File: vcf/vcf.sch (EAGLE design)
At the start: 98 parts, among them IC1 OPA4130U, IC2 OPA4130U, IC3 OPA4130U, IC4 OPA4130U, IC5 OPA4130U, Q1 BC847ASMD, Q2 BC847ASMD, Q3 BC847ASMD, Q4 BC847ASMD, Q5 BC847ASMD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

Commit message: made bug fixes.  almost ready to send out again.
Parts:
- removed R21, R27, R28, R43: 1meg, dan:R-US_R0603
- C1: value 1n -> 18n
- C2, C3, C4: value 1n -> 36n
- R23: value 100k -> 10k
- R25, R26: value 10k -> 1k
- R44: value 10k -> 100k
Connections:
- removed net N$43: IC1D.+IN, R43.2, VPEROCT.P$3
- new net N$67: AIN.P$3, GAIN.E
- net GND: no longer R21.1, R27.1, R28.1, R43.1
- net N$18: now also AIN2.P$3, GAIN1.E; no longer AIN.P$3, IC1A.+IN, R21.2
- net N$29: now also R25.1; no longer MODAMT.E
- net N$30: now also R20.1; no longer GAIN1.E
- net N$33: now also MIN.P$3, MODAMT.E; no longer AIN2.P$3, IC1B.+IN, R27.2
- net N$38: now also R26.1; no longer SCALE.E
- net N$40: now also SCALE.E, VPEROCT.P$3; no longer MODAMT.S, R25.1
- net N$41: now also IC1D.+IN; no longer R26.1
- net N$50: now also MODAMT.S; no longer MIN.P$3, R28.2
- net N$57: now also IC1A.+IN; no longer R19.1
- net N$62: now also IC1B.+IN; no longer R20.1
- net N$63: now also R19.1; no longer GAIN.E
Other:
- note added: "make this res bigger"
- note removed: "Freq pot polarity is wrong"
- note removed: "Move the buffers after the pots"
- moved on the sheet: GAIN, GAIN1, IC1A, IC1B, IC1C, IC1D, MODAMT, SCALE

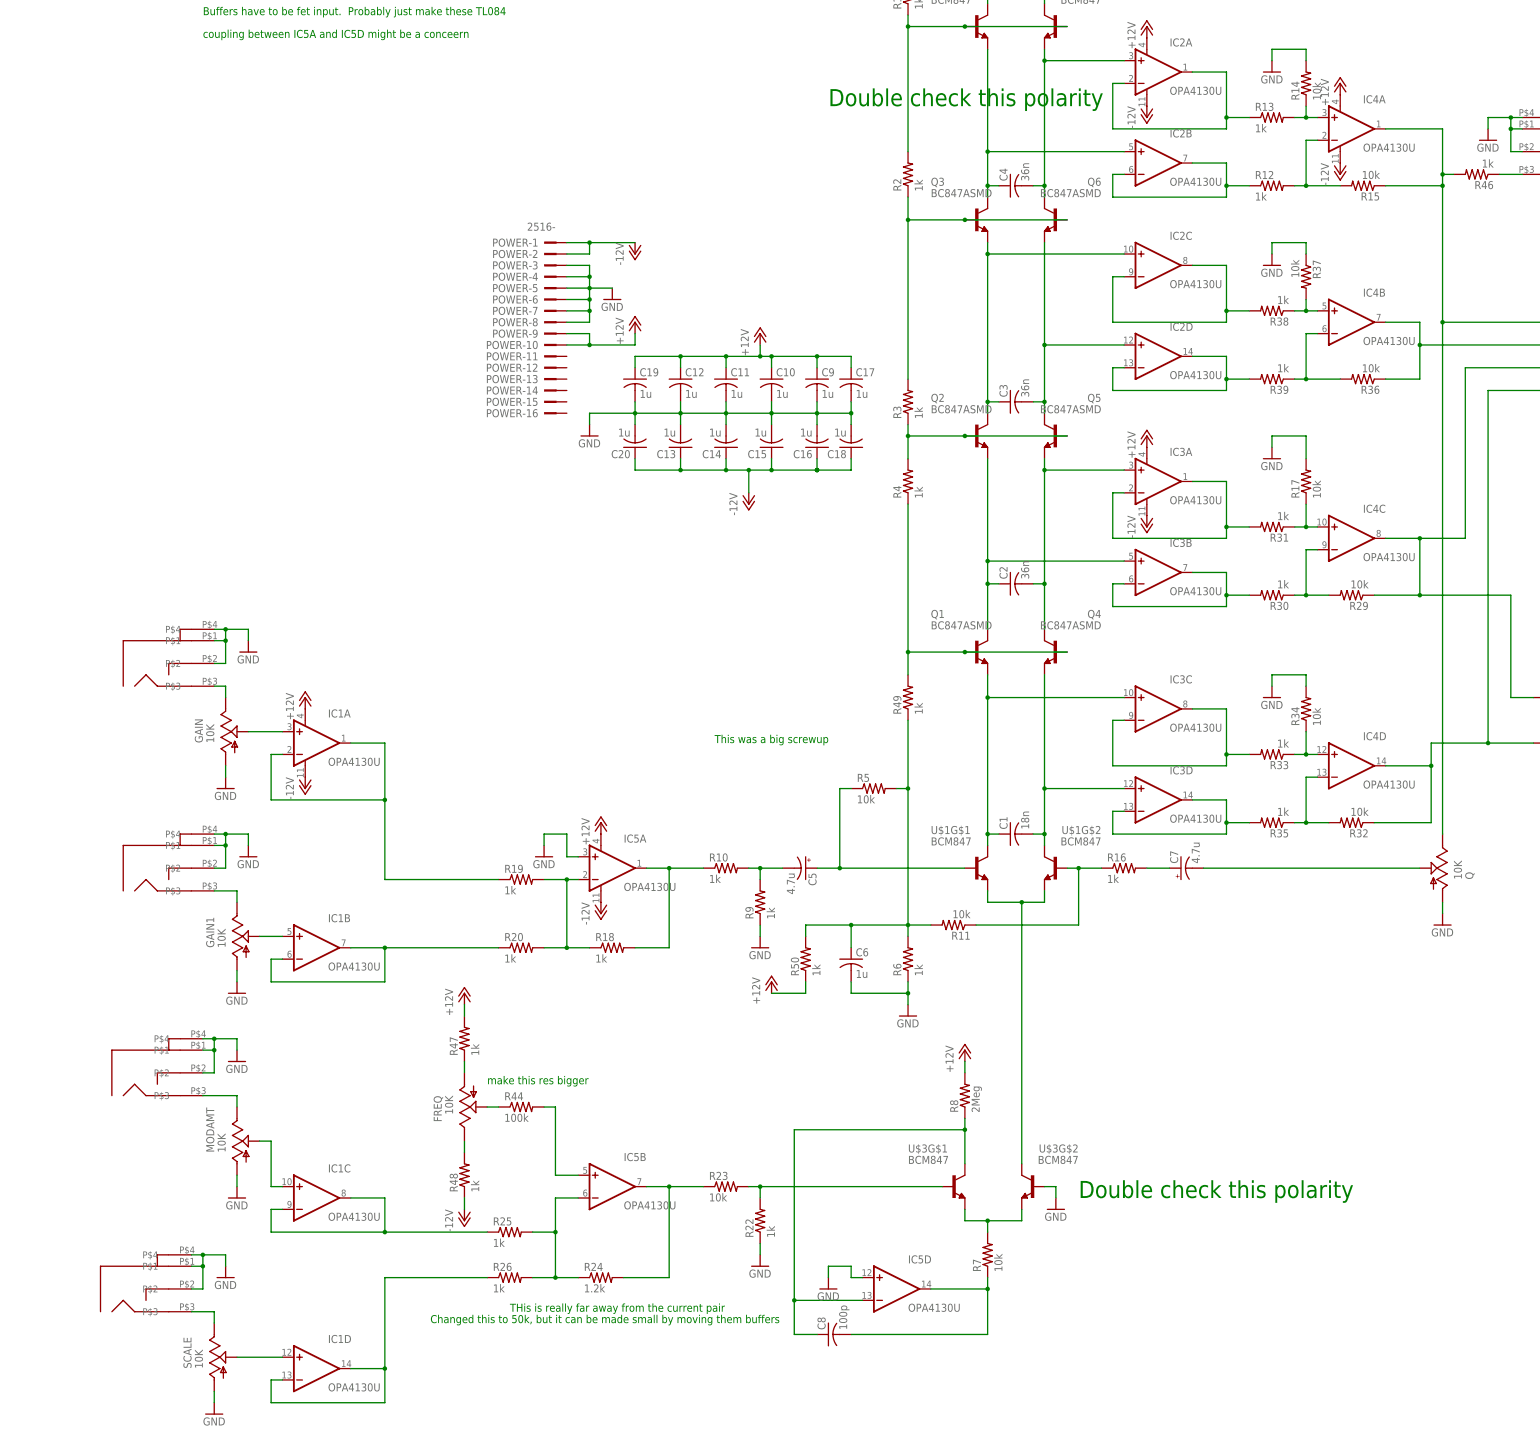
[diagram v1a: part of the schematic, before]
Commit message: fixed the input impedance situation.
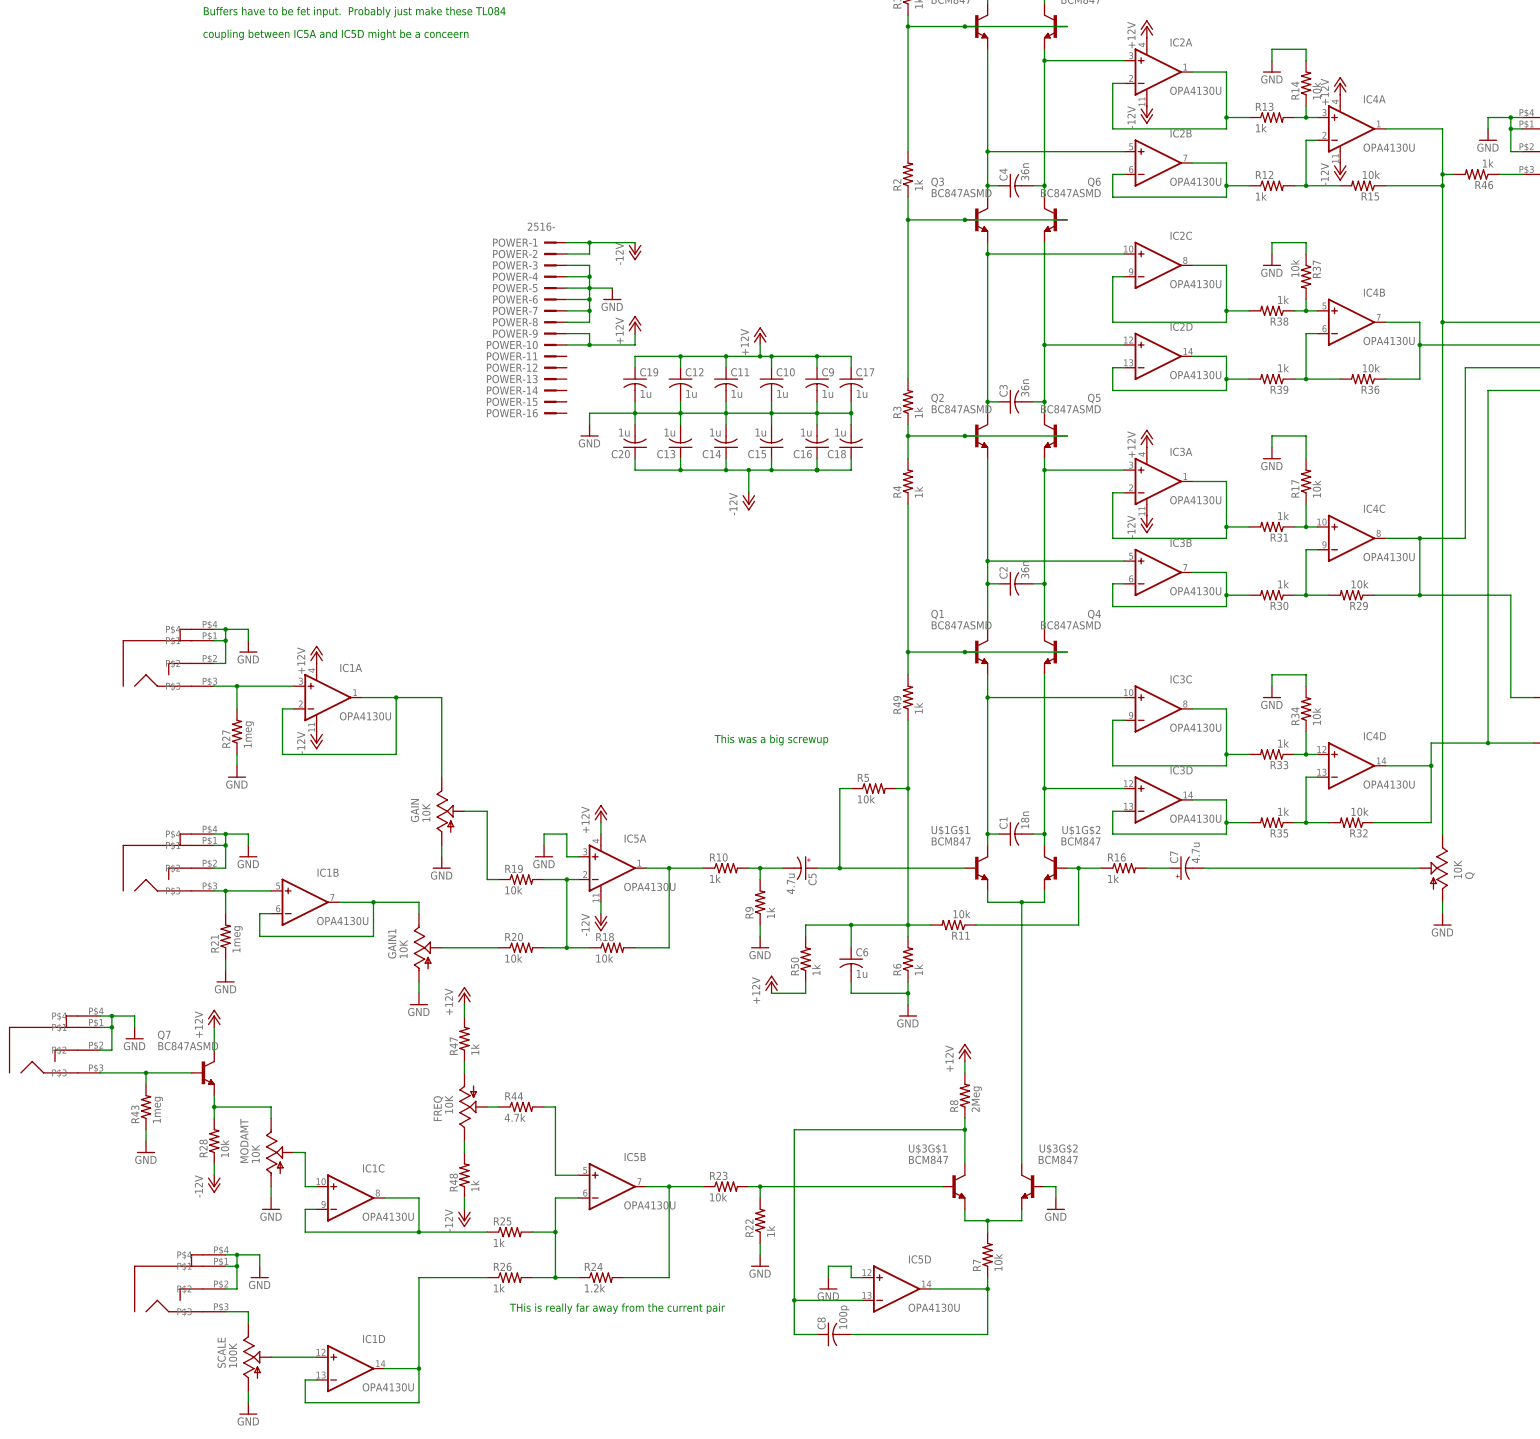
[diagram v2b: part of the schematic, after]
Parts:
- added Q7: BC847ASMD, dan:BC847ASMD
- added R21, R27, R43: 1meg, dan:R-US_R0603
- added R28: 10k, dan:R-US_R0603
- R18, R19, R20: value 1k -> 10k
- R44: value 100k -> 4.7k
- SCALE: value 10K -> 100K
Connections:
- removed net N$63: IC1A.-IN, IC1A.OUT, R19.1
- new net N$43: GAIN.S, R19.1
- new net N$69: AIN2.P$3, IC1B.+IN, R21.2
- net +12V: now also Q7.C
- net -12V: now also R28.1
- net GND: now also R21.1, R27.1, R43.1
- net N$18: now also MIN.P$3, Q7.B, R43.2; no longer AIN2.P$3, GAIN1.E
- net N$30: now also GAIN1.E; no longer R20.1
- net N$33: now also Q7.E, R28.2; no longer MIN.P$3
- net N$57: now also GAIN1.S, R20.1; no longer GAIN.S, IC1A.+IN
- net N$62: now also AIN.P$3, IC1A.+IN, R27.2; no longer GAIN1.S, IC1B.+IN
- net N$67: now also IC1A.-IN, IC1A.OUT; no longer AIN.P$3
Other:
- note removed: "Changed this to 50k, but it can be made small by moving them buffers"
- note removed: "Double check this polarity"
- note removed: "make this res bigger"
- moved on the sheet: GAIN, GAIN1, IC1A, IC1B, IC1C, IC1D, MODAMT, SCALE

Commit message: fixed values in schematic after getting 2nd board rev back.
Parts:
- R10: value 1k -> 10k
- R25: value 1k -> 2.2k
- R26: value 1k -> 4.7k
- R44: value 4.7k -> 10k
- R47, R48: value 1k -> 100k
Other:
- note added: "100k might be a good value for these"
- note removed: "THis is really far away from the current pair"
- note removed: "This was a big screwup"
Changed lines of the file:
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@@
 <part name="R9" library="dan" deviceset="R-US_" device="R0603" value="1k"/>
 <part name="GND4" library="dan" deviceset="GND" device=""/>
-<part name="R10" library="dan" deviceset="R-US_" device="R0603" value="1k"/>
+<part name="R10" library="dan" deviceset="R-US_" device="R0603" value="10k"/>
 <part name="R11" library="dan" deviceset="R-US_" device="R0603" value="10k"/>
 <part name="P+3" library="dan" deviceset="+12V" device=""/>
@@
 <part name="R23" library="dan" deviceset="R-US_" device="R0603" value="10k"/>
 <part name="R24" library="dan" deviceset="R-US_" device="R0603" value="1.2k"/>
-<part name="R25" library="dan" deviceset="R-US_" device="R0603" value="1k"/>
-<part name="R26" library="dan" deviceset="R-US_" device="R0603" value="1k"/>
+<part name="R25" library="dan" deviceset="R-US_" device="R0603" value="2.2k"/>
+<part name="R26" library="dan" deviceset="R-US_" device="R0603" value="4.7k"/>
 <part name="MODAMT" library="dan" deviceset="US-EVU" device="F2J" value="10K"/>
 <part name="GND11" library="dan" deviceset="GND" device=""/>
@@
 <part name="P-7" library="dan" deviceset="-12V" device=""/>
 <part name="P+9" library="dan" deviceset="+12V" device=""/>
-<part name="R44" library="dan" deviceset="R-US_" device="R0603" value="4.7k"/>
+<part name="R44" library="dan" deviceset="R-US_" device="R0603" value="10k"/>
 <part name="GAIN1" library="dan" deviceset="US-EVU" device="F2J" value="10K"/>
 <part name="C5" library="dan" deviceset="CPOL-US" device="E2.5-6" value="4.7u"/>
@@
 <part name="R45" library="dan" deviceset="R-US_" device="R0603" value="1k"/>
 <part name="R46" library="dan" deviceset="R-US_" device="R0603" value="1k"/>
-<part name="R47" library="dan" deviceset="R-US_" device="R0603" value="1k"/>
-<part name="R48" library="dan" deviceset="R-US_" device="R0603" value="1k"/>
+<part name="R47" library="dan" deviceset="R-US_" device="R0603" value="100k"/>
+<part name="R48" library="dan" deviceset="R-US_" device="R0603" value="100k"/>
 <part name="R49" library="dan" deviceset="R-US_" device="R0603" value="1k"/>
 <part name="P+11" library="dan" deviceset="+12V" device=""/>
@@
 <text x="-137.16" y="228.6" size="1.778" layer="91">Buffers have to be fet input.  Probably just make these TL084</text>
 <text x="-137.16" y="223.52" size="1.778" layer="91">coupling between IC5A and IC5D might be a conceern</text>
-<text x="-68.58" y="-60.96" size="1.778" layer="91">THis is really far away from the current pair</text>
-<text x="-22.86" y="66.04" size="1.778" layer="91">This was a big screwup</text>
+<text x="-73.66" y="-2.54" size="1.778" layer="91">100k might be a good value for these</text>
 </plain>
 <instances>

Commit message: added a vca.  made changes to the filter components
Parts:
- added C21, C22: 10u, dan:CPOL-USE2.5-6
- added R51: 10, dan:R-US_R0603
- C5: value 4.7u -> 10u
- R10, R14, R15, R17, R19, R20, R29, R32, R34, R36, R37: value 10k -> 47k
- R44: value 10k -> 470k
- R47, R48: value 100k -> 22k
- R50: value 1k -> dnp
- R9: value 1k -> 10
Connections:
- new net N$63: C21.+, R46.2
- new net N$70: C22.+, R45.2
- new net N$71: POWER-10.KL, POWER-9.KL, R51.2
- new net N$72: POWER-1.KL, POWER-2.KL, R9.2
- net +12V: now also R51.1; no longer POWER-10.KL, POWER-9.KL
- net -12V: now also R9.1; no longer POWER-1.KL, POWER-2.KL
- net GND: no longer R9.1
- net N$14: now also R10.2; no longer C5.+
- net N$20: now also C5.-; no longer R10.1
- net N$21: now also C5.+, R10.1; no longer C5.-, R10.2, R9.2
- net N$27: now also C21.-; no longer R46.2
- net N$61: now also C22.-; no longer R45.2
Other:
- note added: "Make the instrumentation amps and summing amps opa4134"
- note added: "These gain resistors unverified"
- note added: "need to figure these out. 22k?"
- note added: "try 47k for these"
- note removed: "100k might be a good value for these"
- note removed: "Make sure the buffers don't share packages with the instrumentation amps."
- note removed: "coupling between IC5A and IC5D might be a conceern"
- moved on the sheet: C5, R10, R45, R46, R9
